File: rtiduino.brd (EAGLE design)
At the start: 181.8 x 126 mm, 139 parts, among them J1 DCJ0202, J2 3.5MM-JACK, J3 2.5MM-JACKPRO, J4 USB PROG, Q2 16MHz, U1 ATMEGA2560AU, U10 AQV252G, U11 AQV252G, U12 AQV252G, U13 AQV252G, U14 AQV252G, U15 AQV252G, U16 AQV252G, U17 AQV252G, U2 FT232RL, U20 AQV252G, U21 AQV252G, U22 AQV252G, U23 AQV252G, U24 AQV252G, U25 AQV252G, U26 AQV252G, U27 AQV252G, U3 LM2594HVM-5.0, U30 AQV252G, U31 AQV252G, U32 AQV252G, U33 AQV252G, U34 AQV252G, U35 AQV252G, U36 AQV252G, U37 AQV252G, U4 FT232RL, U5 FOD852, U6 LED-DRIVER

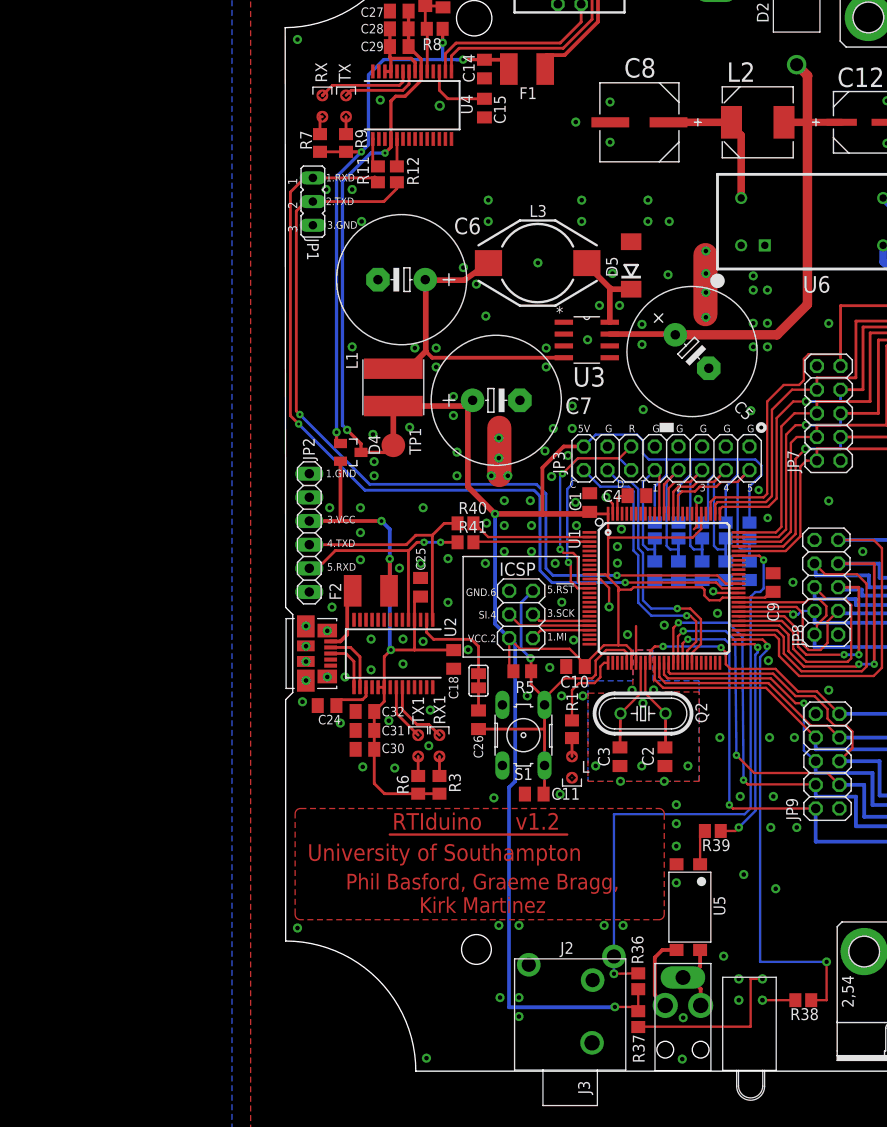
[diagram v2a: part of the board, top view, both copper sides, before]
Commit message: Tweak to camera shutter trigger (split focus and shutter), tweak to serial programming, misc fixes
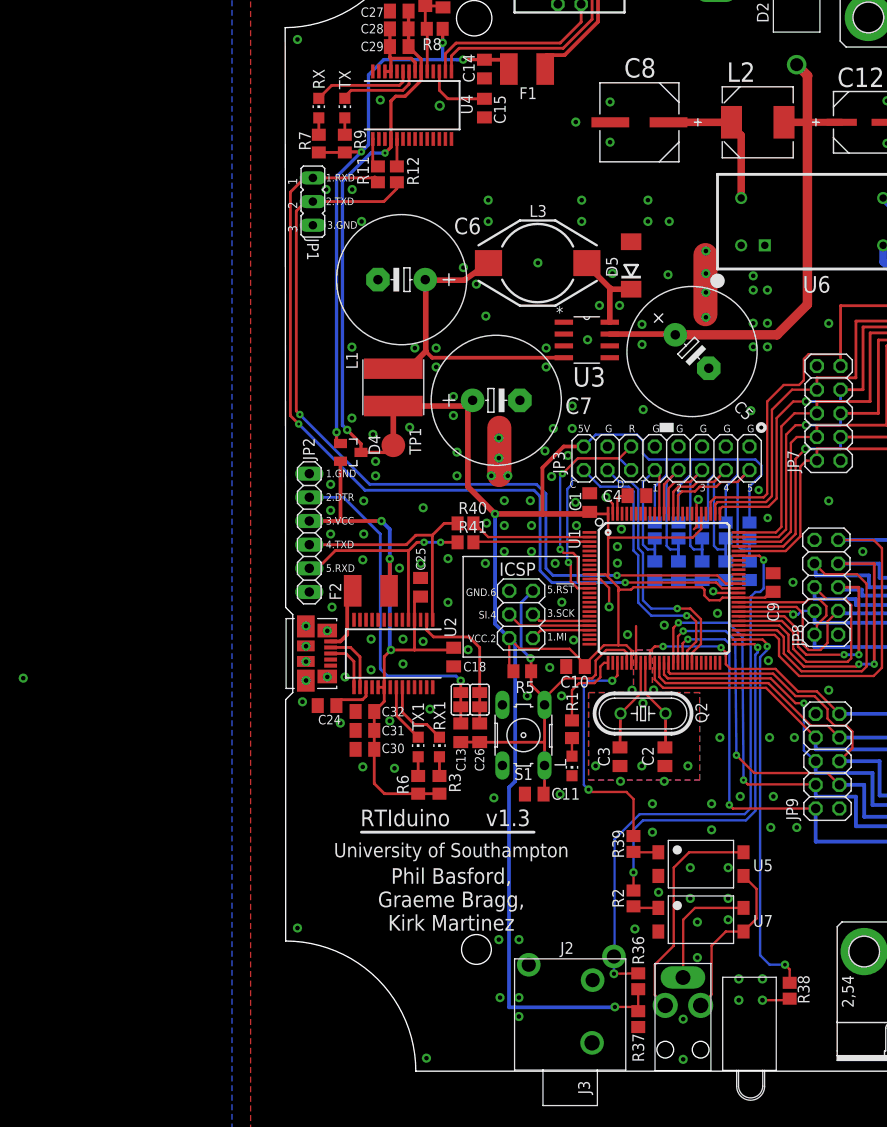
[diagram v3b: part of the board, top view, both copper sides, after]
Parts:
- added C13: 100nF, rcl:C0805K
- added R2: 560, resistor:R0805
- added RESET-EN1: (no value), jumper:SJ
- added U7: FOD852, RTI:DIP4-SMD
- L, RX, RX1, TX, TX1: device led:0805RND -> led:CHIP-LED0805
- moved R39 8.63 mm to (37.3, 24.4), turned to 270 degrees
- moved U5 6.19 mm to (44.6, 22.2), turned to 0 degrees
- moved RESET-EN 2.04 mm to (20.8, 39.9)
- moved R38 1.78 mm to (54.1, 8.64), turned to 270 degrees
- moved C26 1.40 mm to (20.8, 36.3)
- moved RX 0.44 mm to (3.56, 103.4), turned to 0 degrees
- moved C18 0.25 mm to (18.0, 44.5)
- moved TX 0.25 mm to (6.35, 103.4), turned to 0 degrees
- moved R9 0.15 mm to (6.35, 99.6)
- moved R7 0.15 mm to (3.56, 99.6)
- moved L 0.13 mm to (30.7, 32.8), turned to 180 degrees
- moved RX1 0.13 mm to (16.5, 34.8), turned to 0 degrees
- moved TX1 0.13 mm to (14.2, 34.8), turned to 0 degrees
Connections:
- net N$66 renamed DTR
- removed net N$51: J3.R, J3.T, U5.P$4
- new net CAM_GND: J3.SLEEVE, U5.P$3, U7.P$3
- new net CAM_RING: J3.RING, U5.P$4
- new net CAM_SHUTTER: J3.TIP, U7.P$4
- new net DTRP: C13.1, JP2.2, RESET-EN1.1, RESET-EN1.2
- new net FOCUS: R39.1, U1.28
- net GND: now also L.C, U7.P$2; no longer L.P$2
- net N$15: now also RX.C; no longer RX.P$2
- net N$2: now also L.A; no longer L.P$1
- net N$50: now also RX1.C; no longer RX1.P$2
- net N$52: now also TX1.C; no longer TX1.P$2
- net N$53: now also TX.C; no longer TX.P$2
- net N$54: now also RX.A; no longer RX.P$1
- net N$55: now also TX.A; no longer TX.P$1
- net N$58: now also RX1.A; no longer RX1.P$1
- net N$61: now also R2.2, U7.P$1; no longer J3.S, U5.P$3
- net N$62: now also TX1.A; no longer TX1.P$1
- net RESET: now also C13.2
- net SHUTTER: now also R2.1; no longer R39.1
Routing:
- net DTRP: track 0.00 -> 37.5 mm, vias 0 -> 1
- net FOCUS: track 0.00 -> 26.0 mm, vias 0 -> 2
- net CAM_RING: track 0.00 -> 24.3 mm
- net N$56: track 19.1 -> 0.00 mm
- net N$44: track 19.0 -> 0.00 mm
- net CAM_GND: track 0.00 -> 18.1 mm
- net SHUTTER: track 24.5 -> 40.3 mm
- net CAM_SHUTTER: track 0.00 -> 13.2 mm
- net RUNNING: track 50.6 -> 42.2 mm
- net N$51: track 7.62 -> 0.00 mm
- net N$61: track 8.27 -> 2.74 mm
- net RESET: track 44.4 -> 46.3 mm
- net FIRE: track 65.1 -> 63.5 mm
- net DTR: track 14.4 -> 15.7 mm
- net N$59: track 3.79 -> 2.69 mm
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- removed copper zone on layer 1, net N$3
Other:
- board text added: "2.DTR"
- board text added: "v1.3"
- board text removed: "U5"
- board text removed: "v1.2"

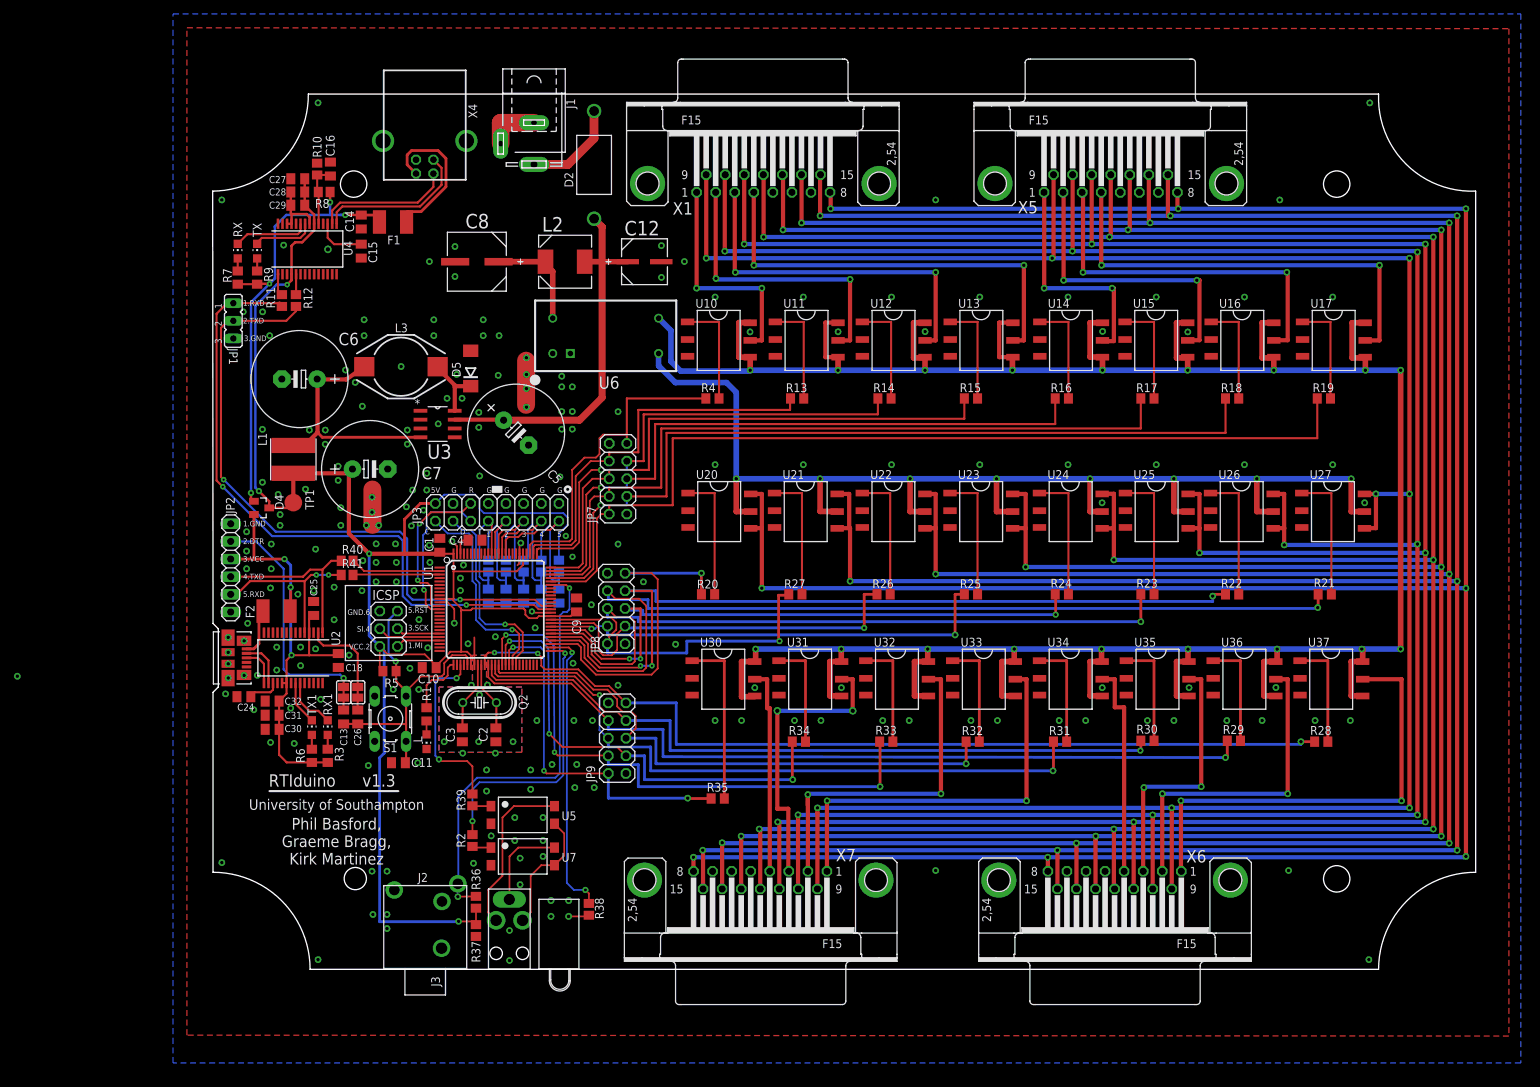
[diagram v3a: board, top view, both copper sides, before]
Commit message: Version 1.3 of RTIDuino and updated order sheet
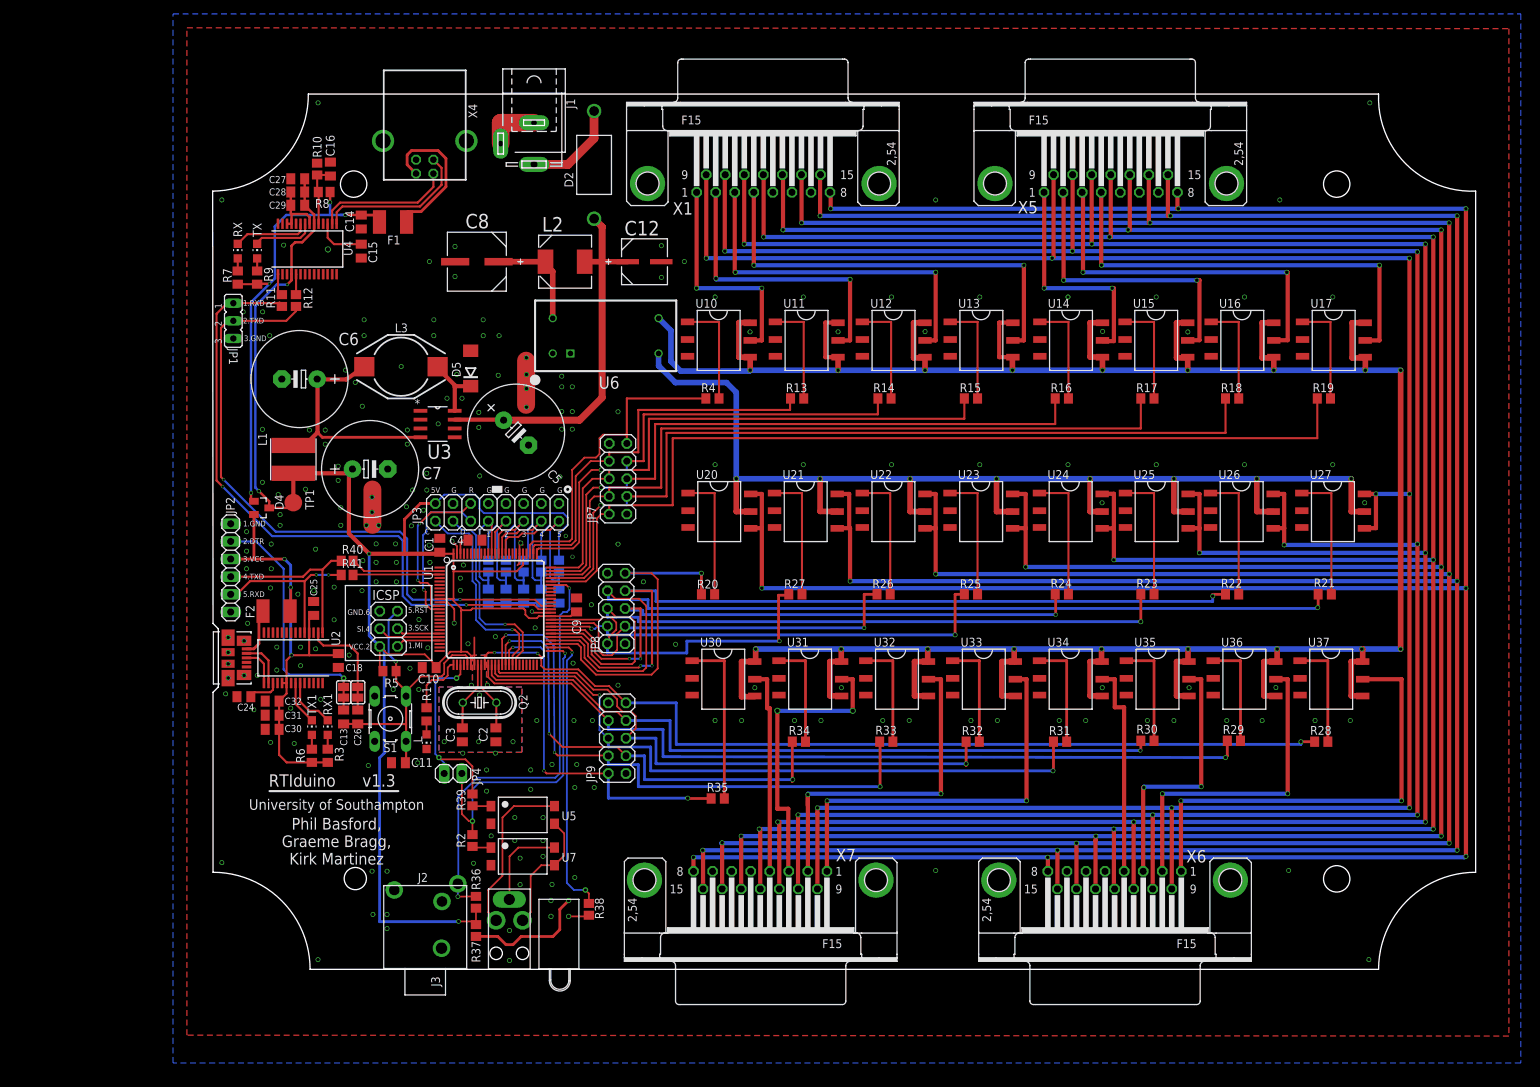
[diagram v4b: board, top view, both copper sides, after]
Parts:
- added JP4: (no value), pinhead:1X02
- C1, C10, C14, C15, C16, C4, C42, C43, C44, C45, C46, C9: value 100n -> 100nF
- C11, C2, C3: value 22p -> 22pF
- C12: value 10UF -> 10uF
- C8: value 47UF -> 47uF
- R3, R6, R7, R9: value 1k -> 1K
- R42, R43, R44, R45, R46: value 10k -> 10K
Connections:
- net N$11 renamed A4_30V
- net N$14 renamed C6_30V
- net N$33 renamed A0_30V
- net N$34 renamed C0_30V
- net N$35 renamed A1_30V
- net N$36 renamed A2_30V
- net N$37 renamed A3_30V
- net N$38 renamed C2_30V
- net N$39 renamed C3_30V
- net N$40 renamed C4_30V
- net N$41 renamed C5_30V
- net N$42 renamed C7_30V
- net N$45 renamed A5_30V
- net N$46 renamed A6_30V
- net N$47 renamed A7_30V
- net N$49 renamed C1_30V
- net FOCUS: now also JP4.1
- net SHUTTER: now also JP4.2
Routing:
- net N$56: track 0.00 -> 18.2 mm
- net SHUTTER: track 40.3 -> 48.1 mm
- net FOCUS: track 26.0 -> 28.5 mm
- net GND: vias 225 -> 226
